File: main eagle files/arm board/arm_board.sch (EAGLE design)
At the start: 75 parts, among them J1 APPPP45_PCB_HORIZ_RIGHT, J10 APPPP45_PCB_HORIZ_RIGHT, J11 APPPP45_PCB_HORIZ_RIGHT, J12 APPPP45_PCB_HORIZ_RIGHT, J13 APPPP45_PCB_HORIZ_RIGHT, J2 APPPP45_PCB_HORIZ_RIGHT, J3 APPPP45_PCB_HORIZ_RIGHT, J4 APPPP45_PCB_HORIZ_RIGHT, J5 APPPP45_PCB_HORIZ_RIGHT, J6 APPPP45_PCB_HORIZ_RIGHT, J7 APPPP45_PCB_HORIZ_RIGHT, J8 APPPP45_PCB_HORIZ_RIGHT, J9 APPPP45_PCB_HORIZ_RIGHT, Q1 Q_IRF7437SMD, U1 TIVA-1294, U2 XBEE_802.15.4SMD

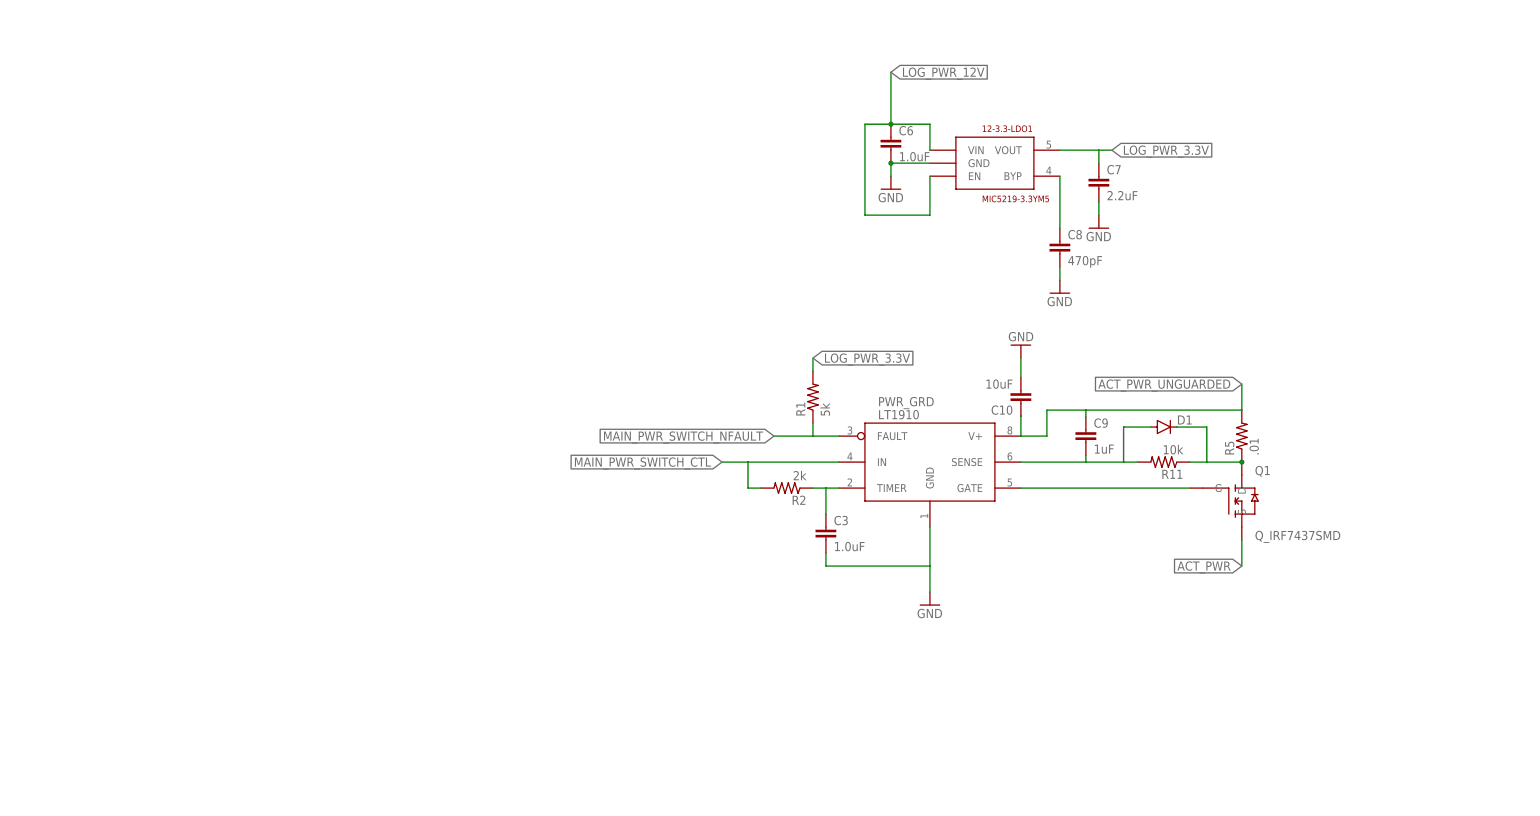
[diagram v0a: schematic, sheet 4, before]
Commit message: Correcting schematic issue, adding preliminary board.
The previous power guarding method -- using the LT1910 to current sense
and also turn off the power line at the same time -- wasn't going to
work as its current sensing was way too small. Instead I've replaced
that part of the process with an actual current sensor to let the
microcontroller know when we've had an overcurrent condition.
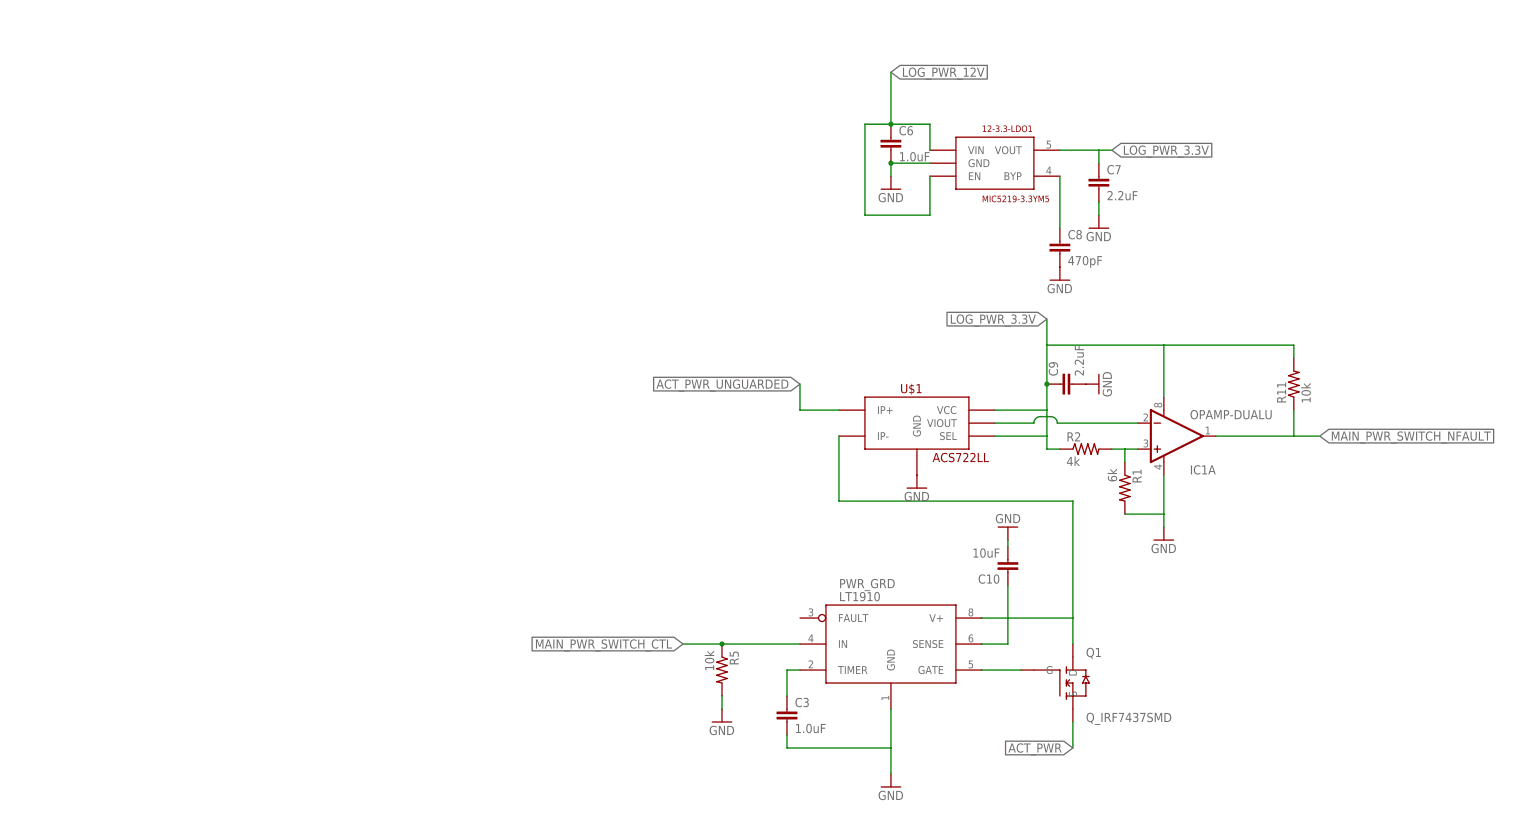
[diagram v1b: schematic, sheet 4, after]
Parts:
- removed D1: (no value), MRDT-EAGLE-Training:DIODESMA
- added IC1: OPAMP-DUALU, SparkFun-AnalogIC:OPAMP-DUALU
- added U$1: ACS722LL, lin reg:ACS722LL
- C9: value 1uF -> 2.2uF; device SparkFun-Capacitors:1UF-25V-10%(0805) -> SparkFun-Capacitors:0.1UF-25V(+80/-20%)(0603)
- R1: value 5k -> 6k
- R11: device SparkFun-Passives:RESISTOR0805-RES -> SparkFun-Passives:RESISTOR0603-RES
- R2: value 2k -> 4k
- R5: value .01 -> 10k; device SparkFun-Passives:RESISTOR0805-RES -> SparkFun-Passives:RESISTOR0603-RES
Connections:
- removed net N$4: D1.C, Q1.D, R11.1, R5.1
- new net $N3: C10.1, PWR_GRD.SENSE, PWR_GRD.V+, Q1.D, U$1.IP-
- new net N$7: IC1A.+IN, R1.1, R2.2
- net ACT_PWR_UNGUARDED: now also U$1.IP+; no longer C9.1, PWR_GRD.V+, R5.2
- net GND: now also C9.2, IC1A.V-, R1.2, R5.2, U$1.GND
- net LOG_PWR_3.3V: now also C9.1, IC1A.V+, R11.2, R2.1, U$1.SEL, U$1.VCC; no longer R1.2
- net MAIN_PWR_SWITCH_CTL: now also R5.1; no longer R2.2
- net MAIN_PWR_SWITCH_NFAULT: now also IC1A.OUT, R11.1; no longer PWR_GRD.FAULT, R1.1
- net N$1: no longer R2.1
- net N$5: now also IC1A.-IN, U$1.VIOUT; no longer C9.2, D1.A, PWR_GRD.SENSE, R11.2
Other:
- moved on the sheet: C10, C3, C9, PWR_GRD, Q1, R1, R11, R2, R5

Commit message: Version 1.0-alpha ready for review
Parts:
- renumbered 12-3.3-LDO1 to U$2, PWR_GRD to U$0
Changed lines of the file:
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@@
 <?xml version="1.0" encoding="utf-8"?>
 <!DOCTYPE eagle SYSTEM "eagle.dtd">
-<eagle version="7.4.0">
+<eagle version="6.5.0">
 <drawing>
 <settings>
@@
 <part name="C55" library="SparkFun-Capacitors" deviceset="0.1UF-25V(+80/-20%)(0603)" device="" value=".01uF"/>
 <part name="GND63" library="SparkFun-Aesthetics" deviceset="GND" device=""/>
-<part name="12-3.3-LDO1" library="lin reg" deviceset="MIC5219-3.3YM5" device=""/>
+<part name="U$2" library="lin reg" deviceset="MIC5219-3.3YM5" device=""/>
 <part name="GND19" library="SparkFun-Aesthetics" deviceset="GND" device=""/>
 <part name="C6" library="SparkFun-Capacitors" deviceset="1.0UF-16V-10%(0603)" device="" value="1.0uF"/>
@@
 <part name="U1" library="MRDT-Microcontrollers" deviceset="TIVA-1294" device=""/>
 <part name="GND12" library="SparkFun-Aesthetics" deviceset="GND" device=""/>
-<part name="PWR_GRD" library="MRDT-2015-PowerBoard" deviceset="LT1910" device=""/>
+<part name="U$0" library="MRDT-2015-PowerBoard" deviceset="LT1910" device=""/>
 <part name="C3" library="SparkFun-Capacitors" deviceset="1.0UF-16V-10%(0603)" device="" value="1.0uF"/>
 <part name="GND14" library="SparkFun-Aesthetics" deviceset="GND" device=""/>
@@
 </plain>
 <instances>
-<instance part="12-3.3-LDO1" gate="G$1" x="17.78" y="27.94"/>
+<instance part="U$2" gate="G$1" x="17.78" y="27.94"/>
 <instance part="GND19" gate="1" x="-2.54" y="22.86"/>
 <instance part="C6" gate="G$1" x="-2.54" y="30.48"/>
@@
 <instance part="GND20" gate="1" x="38.1" y="15.24"/>
 <instance part="GND21" gate="1" x="30.48" y="5.08"/>
-<instance part="PWR_GRD" gate="G$1" x="-2.54" y="-73.66"/>
+<instance part="U$0" gate="G$1" x="-2.54" y="-73.66"/>
 <instance part="C3" gate="G$1" x="-22.86" y="-81.28"/>
 <instance part="GND14" gate="1" x="-2.54" y="-93.98"/>
@@
 <net name="GND" class="0">
 <segment>
-<pinref part="12-3.3-LDO1" gate="G$1" pin="GND"/>
+<pinref part="U$2" gate="G$1" pin="GND"/>
 <wire x1="5.08" y1="27.94" x2="-2.54" y2="27.94" width="0.1524" layer="91"/>
 <wire x1="-2.54" y1="27.94" x2="-2.54" y2="25.4" width="0.1524" layer="91"/>
@@
 <pinref part="C3" gate="G$1" pin="2"/>
 <wire x1="-22.86" y1="-83.82" x2="-22.86" y2="-86.36" width="0.1524" layer="91"/>
-<pinref part="PWR_GRD" gate="G$1" pin="GND"/>
+<pinref part="U$0" gate="G$1" pin="GND"/>
 <wire x1="-22.86" y1="-86.36" x2="-2.54" y2="-86.36" width="0.1524" layer="91"/>
 <wire x1="-2.54" y1="-86.36" x2="-2.54" y2="-78.74" width="0.1524" layer="91"/>
@@
 <segment>
 <wire x1="-2.54" y1="35.56" x2="-2.54" y2="45.72" width="0.1524" layer="91"/>
-<pinref part="12-3.3-LDO1" gate="G$1" pin="VIN"/>
+<pinref part="U$2" gate="G$1" pin="VIN"/>
 <wire x1="5.08" y1="30.48" x2="5.08" y2="35.56" width="0.1524" layer="91"/>
 <wire x1="5.08" y1="35.56" x2="-2.54" y2="35.56" width="0.1524" layer="91"/>
 <label x="-2.54" y="45.72" size="1.778" layer="95" xref="yes"/>
-<pinref part="12-3.3-LDO1" gate="G$1" pin="EN"/>
+<pinref part="U$2" gate="G$1" pin="EN"/>
 <wire x1="5.08" y1="25.4" x2="5.08" y2="17.78" width="0.1524" layer="91"/>
 <wire x1="5.08" y1="17.78" x2="-7.62" y2="17.78" width="0.1524" layer="91"/>
@@
 <label x="40.64" y="30.48" size="1.778" layer="95" xref="yes"/>
 <pinref part="C7" gate="G$1" pin="1"/>
-<pinref part="12-3.3-LDO1" gate="G$1" pin="VOUT"/>
+<pinref part="U$2" gate="G$1" pin="VOUT"/>
 <wire x1="30.48" y1="30.48" x2="38.1" y2="30.48" width="0.1524" layer="91"/>
 <wire x1="40.64" y1="30.48" x2="38.1" y2="30.48" width="0.1524" layer="91"/>
@@
 <net name="N$2" class="0">
 <segment>
-<pinref part="12-3.3-LDO1" gate="G$1" pin="BYP"/>
+<pinref part="U$2" gate="G$1" pin="BYP"/>
 <pinref part="C8" gate="G$1" pin="1"/>
 <wire x1="30.48" y1="15.24" x2="30.48" y2="25.4" width="0.1524" layer="91"/>
@@
 <net name="MAIN_PWR_SWITCH_CTL" class="0">
 <segment>
-<pinref part="PWR_GRD" gate="G$1" pin="IN"/>
+<pinref part="U$0" gate="G$1" pin="IN"/>
 <wire x1="-20.32" y1="-66.04" x2="-35.56" y2="-66.04" width="0.1524" layer="91"/>
 <label x="-43.18" y="-66.04" size="1.778" layer="95" rot="R180" xref="yes"/>
@@
 <net name="N$1" class="0">
 <segment>
-<pinref part="PWR_GRD" gate="G$1" pin="TIMER"/>
+<pinref part="U$0" gate="G$1" pin="TIMER"/>
 <wire x1="-22.86" y1="-71.12" x2="-20.32" y2="-71.12" width="0.1524" layer="91"/>
 <wire x1="-22.86" y1="-71.12" x2="-22.86" y2="-76.2" width="0.1524" layer="91"/>
@@
 <net name="$N3" class="0">
 <segment>
-<pinref part="PWR_GRD" gate="G$1" pin="V+"/>
+<pinref part="U$0" gate="G$1" pin="V+"/>
 <pinref part="U$1" gate="G$1" pin="IP-"/>
 <wire x1="-12.7" y1="-25.4" x2="-12.7" y2="-38.1" width="0.1524" layer="91"/>
@@
 <wire x1="33.02" y1="-60.96" x2="33.02" y2="-66.04" width="0.1524" layer="91"/>
 <wire x1="15.24" y1="-60.96" x2="20.32" y2="-60.96" width="0.1524" layer="91"/>
-<pinref part="PWR_GRD" gate="G$1" pin="SENSE"/>
+<pinref part="U$0" gate="G$1" pin="SENSE"/>
 <wire x1="20.32" y1="-60.96" x2="33.02" y2="-60.96" width="0.1524" layer="91"/>
 <wire x1="15.24" y1="-66.04" x2="20.32" y2="-66.04" width="0.1524" layer="91"/>
@@
 <segment>
 <pinref part="Q1" gate="G$1" pin="G"/>
-<pinref part="PWR_GRD" gate="G$1" pin="GATE"/>
+<pinref part="U$0" gate="G$1" pin="GATE"/>
 <wire x1="22.86" y1="-71.12" x2="15.24" y2="-71.12" width="0.1524" layer="91"/>
 </segment>

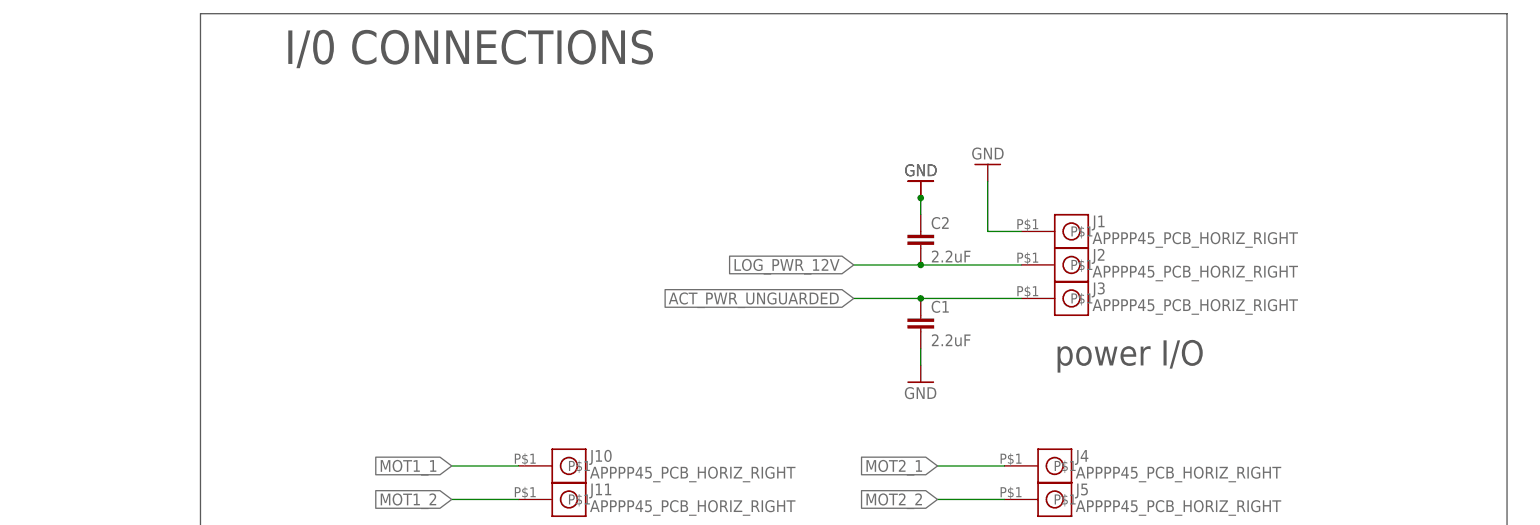
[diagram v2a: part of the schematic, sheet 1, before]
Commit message: Correcting issues, adding powerout to gripper
I changed the tags on the schm to use xref, I messed with the brd to get
rid of erc errors, I redid the power lines going to and from the H
bridges so now it has a total of .04 inches of trace width going to and
from it, and I resized the board so that the sideways andersons would
fit on it.

Still need to put on mounting holes
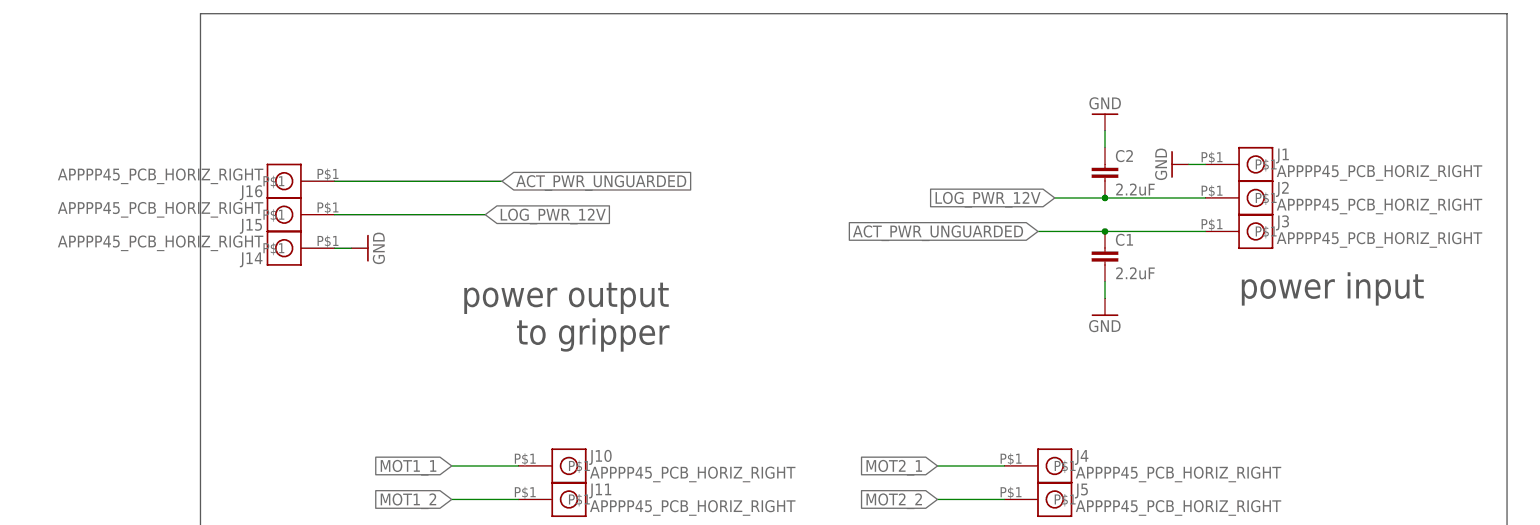
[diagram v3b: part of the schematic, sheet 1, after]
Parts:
- added J14, J15, J16: APPPP45_PCB_HORIZ_RIGHT, MRDT-Connectors:APPPP45_PCB_HORIZ_RIGHT
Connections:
- net ACT_PWR_UNGUARDED: now also J16.P$1
- net GND: now also J14.P$1
- net LOG_PWR_12V: now also J15.P$1
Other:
- note added: "power input"
- note added: "power output to gripper"
- note removed: "I/0 CONNECTIONS"
- note removed: "power I/O"
- moved on the sheet: C1, C2, J1, J2, J3

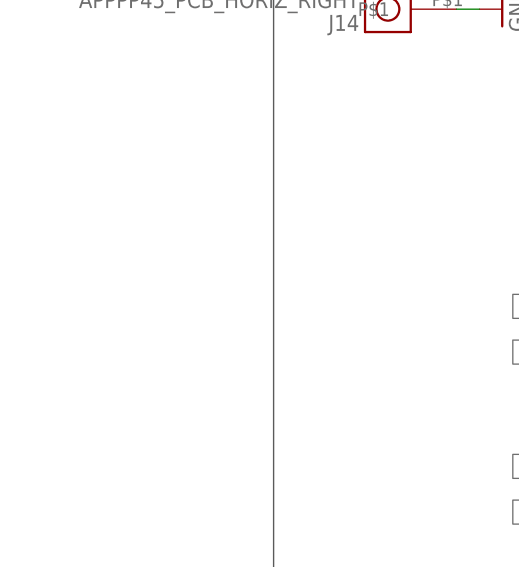
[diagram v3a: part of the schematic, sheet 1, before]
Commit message: added mounting holes
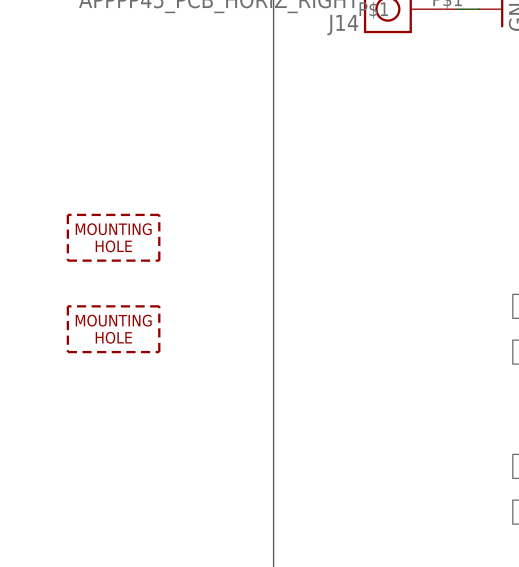
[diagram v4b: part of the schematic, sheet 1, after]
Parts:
- added H1, H2: MOUNTING_HOLE#4, MRDT-Hardware:MOUNTING_HOLE#4
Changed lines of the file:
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@@
 <part name="J16" library="MRDT-Connectors" deviceset="APP" device="PP45_PCB_HORIZ_RIGHT"/>
 <part name="GND4" library="SparkFun-Aesthetics" deviceset="GND" device=""/>
+<part name="H1" library="MRDT-Hardware" deviceset="MOUNTING_HOLE" device="#4"/>
+<part name="H2" library="MRDT-Hardware" deviceset="MOUNTING_HOLE" device="#4"/>
 </parts>
 <sheets>
@@
 <instance part="J16" gate="G$1" x="-66.04" y="101.6" rot="R180"/>
 <instance part="GND4" gate="1" x="-53.34" y="91.44" rot="R90"/>
+<instance part="H1" gate="G$1" x="-101.6" y="63.5"/>
+<instance part="H2" gate="G$1" x="-101.6" y="53.34"/>
 </instances>
 <busses>

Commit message: added mrdt logo
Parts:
- added LOGO1: MRDT_LOGO, MRDT-Hardware:MRDT_LOGO
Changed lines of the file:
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@@
 <part name="H1" library="MRDT-Hardware" deviceset="MOUNTING_HOLE" device="#4"/>
 <part name="H2" library="MRDT-Hardware" deviceset="MOUNTING_HOLE" device="#4"/>
+<part name="LOGO1" library="MRDT-Hardware" deviceset="MRDT_LOGO" device=""/>
 </parts>
 <sheets>
@@
 <instance part="H1" gate="G$1" x="-101.6" y="63.5"/>
 <instance part="H2" gate="G$1" x="-101.6" y="53.34"/>
+<instance part="LOGO1" gate="G$1" x="-101.6" y="43.18"/>
 </instances>
 <busses>

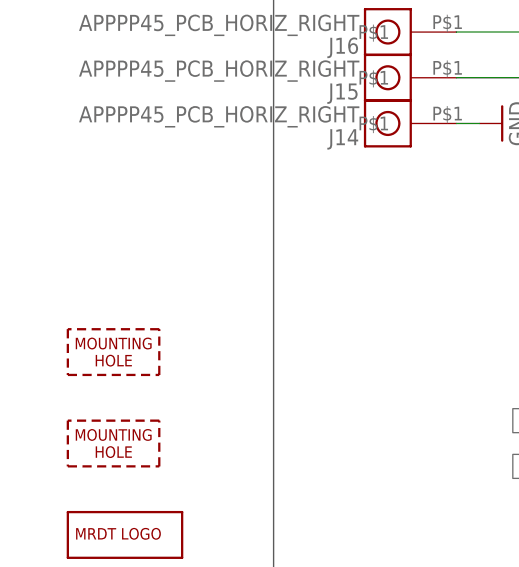
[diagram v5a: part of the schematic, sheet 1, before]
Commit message: adding a third mounting hole
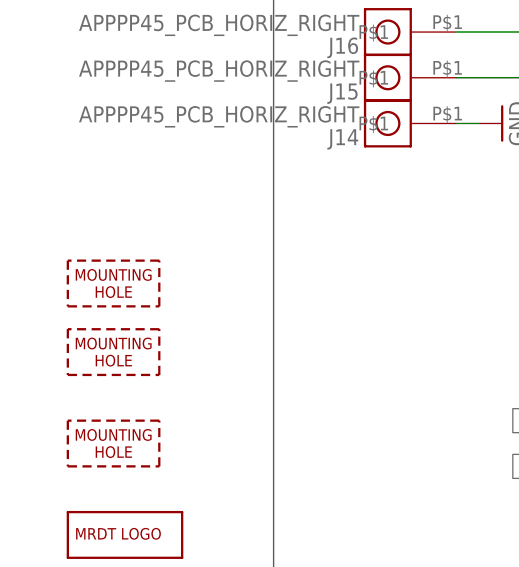
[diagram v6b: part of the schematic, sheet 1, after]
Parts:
- added H3: MOUNTING_HOLE#4, MRDT-Hardware:MOUNTING_HOLE#4
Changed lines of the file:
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@@
 <part name="H2" library="MRDT-Hardware" deviceset="MOUNTING_HOLE" device="#4"/>
 <part name="LOGO1" library="MRDT-Hardware" deviceset="MRDT_LOGO" device=""/>
+<part name="H3" library="MRDT-Hardware" deviceset="MOUNTING_HOLE" device="#4"/>
 </parts>
 <sheets>
@@
 <instance part="H2" gate="G$1" x="-101.6" y="53.34"/>
 <instance part="LOGO1" gate="G$1" x="-101.6" y="43.18"/>
+<instance part="H3" gate="G$1" x="-101.6" y="71.12"/>
 </instances>
 <busses>
